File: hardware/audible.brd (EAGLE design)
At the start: 27.7 x 23.4 mm, 5 parts, among them J1 SQUALL_HEADER, J2 HIROSE-DF40C-10DP-0.4V, J3 HIROSE-DF40C-10DP-0.4V, J5 TC2030-JLINK-NL

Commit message: Almost completed schematic
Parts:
- added C1, C2, C3: 1uF, passives:0402_CAP
- added C4: 100n, passives:0402_CAP
- added C5: 1u, passives:0402_CAP
- added C6: 22uF, passives:0402_CAP
- added IC1: LTC1966CMS8, chips:MSOP8
- added R1, R4: 14k, passives:0402_RES
- added R2, R5: 1k, passives:0402_RES
- added R3: 47k, passives:0402_RES
- added R6: 20k, passives:0402_RES
- added R7, R8, R9: 10k, passives:0402_RES
- added U$2: ICS-40310, chips:LGA_CAV3
- added U$3: LD39015, chips:SOT-23-5
- added U1, U2: MAX417ESA+, chips:21-0041B_8
- moved U$1 7.26 mm to (13.8, 8.79)
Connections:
- new net MIC: C3.1, U$2.P$3
- new net MIC_AMP_1: R1.2, U1.1, U1.5
- new net MIC_AMP_2: C4.1, R4.1, U1.7
- new net N$1: C3.2, R3.2, U1.3
- new net N$10: C6.2, R6.2, R7.1, U2.5
- new net N$2: C4.2, IC1.2
- new net N$4: R1.1, R2.2, U1.2
- new net N$5: R4.2, R5.1, U1.6
- new net N$6: R8.1, U2.6
- new net RMS: C5.2, IC1.5, U2.3
- new net RMS_BUF: R6.1, U2.1, U2.2
- new net VREF: C1.1, IC1.3, R2.1, R3.1, R5.2, U$2.P$1, U$3.5
- net A7: now also R7.2, R9.1, U2.7
- net GND: now also C1.2, C2.2, C5.1, C6.1, IC1.1, IC1.4, IC1.6, R8.2, R9.2, U$2.P$2, U$3.2, U1.4, U2.4
- net P23: now also IC1.8
- net VCC: now also C2.1, IC1.7, U$3.1, U1.8, U2.8
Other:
- board text removed: "2016/03/12"
- board text removed: "Accel"
- board text removed: "BLEES"
- board text removed: "D"
- board text removed: "Ghena, Bertoldi, Jones, Pratt, Su"
- board text removed: "Light"
- board text removed: "Pressure"
- board text removed: "Temp Humid"

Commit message: better layout
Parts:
- added C7: 0.01uF, passives:0402_CAP
- added C8: 0.1uF, passives:0402_CAP
- moved IC1 31.1 mm to (19.7, 18.5)
- moved U$3 23.9 mm to (17.2, 8.71), turned to 90 degrees
- moved U1 20.0 mm to (23.8, 10.3), turned to 90 degrees
- moved U2 16.8 mm to (31.5, 16.6), turned to 90 degrees
- moved R4 10.8 mm to (27.8, 11.7)
- moved C3 10.1 mm to (26.7, 5.44), turned to 90 degrees
- moved R8 9.59 mm to (34.7, 14.4), turned to 270 degrees
- moved R3 9.49 mm to (19.1, 3.30), turned to 90 degrees
- moved R1 9.36 mm to (28.4, 5.44), turned to 90 degrees
- moved R6 9.34 mm to (27.4, 19.3)
- moved C5 8.18 mm to (20.5, 15.4), turned to 90 degrees
- moved C6 8.18 mm to (27.3, 15.6), turned to 90 degrees
- moved R9 7.97 mm to (34.7, 17.0), turned to 270 degrees
- moved R7 7.34 mm to (27.4, 17.5)
- moved C1 7.25 mm to (18.5, 5.69), turned to 90 degrees
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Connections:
- net GND: now also C7.1, C8.2
- net VCC: now also C7.2
- net VREF: now also C8.1

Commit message: better schematic
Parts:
- added Q1: FK3503010L, chips:SC85
- moved U$1 17.9 mm to (29.9, 3.66)
- moved R1 10.6 mm to (19.3, 10.9), turned to 180 degrees
- moved R2 5.87 mm to (19.3, 8.79), turned to 180 degrees
- moved C8 4.34 mm to (22.1, 2.44)
- moved R6 4.34 mm to (27.5, 14.9), turned to 90 degrees
- moved C7 3.79 mm to (24.3, 19.1)
- moved C1 3.69 mm to (15.1, 7.11)
- moved U$3 2.00 mm to (15.6, 9.91)
- moved C3 1.68 mm to (27.4, 3.91)
- moved C6 1.63 mm to (27.4, 17.2)
- moved R7 1.63 mm to (27.4, 19.1)
- moved C2 1.44 mm to (16.5, 7.09), turned to 270 degrees
- moved C5 1.37 mm to (21.8, 15.7)
- moved R4 0.98 mm to (27.3, 12.5), turned to 270 degrees
- moved C4 0.84 mm to (19.2, 15.2)
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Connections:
- net GND: now also Q1.2
- net N$10: now also Q1.3
- net P22: now also U$3.3
- net P24: now also Q1.1

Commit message: Updated sch and brd
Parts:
- added C10, C9: 0.1uF, passives:0402_CAP
- moved C2 7.61 mm to (20.0, 13.9), turned to 180 degrees
- moved R7 7.40 mm to (30.9, 12.6)
- moved C1 6.34 mm to (19.2, 2.34), turned to 270 degrees
- moved C4 5.26 mm to (15.5, 18.9)
- moved C6 4.26 mm to (25.8, 13.3), turned to 270 degrees
- moved R2 3.59 mm to (17.4, 5.71), turned to 0 degrees
- moved R1 3.46 mm to (19.5, 7.42), turned to 0 degrees
- moved U2 2.64 mm to (28.9, 17.0), turned to 0 degrees
- moved R6 2.61 mm to (28.7, 12.6), turned to 0 degrees
- moved Q1 2.51 mm to (22.8, 14.2)
- moved C5 2.42 mm to (24.1, 16.6)
- moved R8 2.33 mm to (33.4, 16.3), turned to 0 degrees
- moved R5 2.27 mm to (26.5, 8.13)
- moved U1 2.22 mm to (23.1, 8.23)
- moved R4 2.15 mm to (26.5, 10.5)
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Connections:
- net RMS renamed N$3
- net GND: now also C10.1, C9.1
- net MIC: now also U$2.P$1; no longer U$2.P$3
- net VCC: now also C10.2, C9.2
- net VREF: now also U$2.P$3; no longer U$2.P$1
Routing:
- net GND: track 4.95 -> 0.00 mm, vias 3 -> 0

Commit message: almost routed
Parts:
- moved C10 14.0 mm to (24.1, 18.4), turned to 90 degrees
- moved C9 10.9 mm to (21.0, 15.2), turned to 180 degrees
- moved C1 7.67 mm to (14.6, 8.43), turned to 180 degrees
- moved C4 7.22 mm to (22.3, 16.5), turned to 180 degrees
- moved Q1 6.81 mm to (29.2, 11.9), turned to 0 degrees
- moved R4 5.19 mm to (23.0, 14.3), turned to 0 degrees
- moved C6 3.78 mm to (29.3, 14.7)
- moved R5 3.73 mm to (26.5, 11.9)
- moved R6 3.68 mm to (31.9, 14.4)
- moved C3 3.56 mm to (24.0, 5.74), turned to 0 degrees
- moved C8 2.70 mm to (19.5, 2.67), turned to 0 degrees
- moved R3 2.69 mm to (22.0, 4.57), turned to 90 degrees
- moved R2 2.39 mm to (19.5, 4.50)
- moved U1 1.94 mm to (22.9, 10.2)
- moved C7 1.29 mm to (25.1, 19.7)
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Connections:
- net A5: no longer J3.9
- net A6: no longer J3.7
- net MISO: no longer J3.8
- net MOSI: no longer J3.6
- net P25: no longer J2.8
- net SCL: no longer J3.3
- net SCLK: no longer J3.10
- net SDA: no longer J3.1
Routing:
- net GND: track 0.00 -> 48.6 mm, vias 0 -> 7
- net VREF: track 0.00 -> 47.2 mm, vias 0 -> 2
- net VCC: track 0.00 -> 38.4 mm, vias 0 -> 4
- net A7: track 0.00 -> 18.3 mm, vias 0 -> 1
- net P24: track 0.00 -> 16.6 mm, vias 0 -> 3
- net SWDIO/!RESET: track 0.00 -> 13.5 mm, vias 0 -> 2
- net 5V: track 0.00 -> 13.5 mm, vias 0 -> 2
- net P23: track 0.00 -> 12.7 mm, vias 0 -> 3
- net P22: track 0.00 -> 10.4 mm, vias 0 -> 1
- net MIC_AMP_1: track 0.00 -> 9.03 mm
- net RMS_BUF: track 0.00 -> 8.09 mm
- net SWDCLK: track 0.00 -> 8.00 mm, vias 0 -> 1
- net N$10: track 0.00 -> 7.44 mm
- net N$4: track 0.00 -> 6.19 mm
- net N$5: track 0.00 -> 6.00 mm
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
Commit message: routed
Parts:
- moved C4 4.72 mm to (18.7, 13.5)
- moved U$3 2.76 mm to (17.3, 7.95)
- moved C2 2.46 mm to (19.8, 11.1)
- moved C9 2.14 mm to (21.5, 13.1)
- moved R5 1.41 mm to (26.1, 13.2), turned to 0 degrees
- moved Q1 1.24 mm to (28.1, 11.4)
- moved R4 1.18 mm to (23.3, 13.2)
- moved U1 1.16 mm to (23.5, 9.17)
- moved C3 0.99 mm to (24.6, 4.98)
- moved IC1 0.97 mm to (20.6, 17.5)
- moved C6 0.94 mm to (29.0, 13.8)
- moved R8 0.91 mm to (33.5, 16.7)
- moved R9 0.91 mm to (34.3, 17.9)
- moved U2 0.89 mm to (29.0, 17.3)
- moved C10 0.89 mm to (23.8, 17.5)
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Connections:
- removed net A5: J1.B9
- removed net A6: J1.B7
- removed net MISO: J1.B8
- removed net MOSI: J1.B6
- removed net P25: J1.A8
- removed net SCL: J1.B3
- removed net SCLK: J1.B10
- removed net SDA: J1.B1
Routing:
- net GND: track 48.6 -> 105.1 mm, vias 7 -> 12
- net VCC: track 38.4 -> 62.3 mm, vias 4 -> 3
- net MIC_AMP_2: track 4.03 -> 8.24 mm, vias 0 -> 2
- net P22: track 10.4 -> 14.3 mm
- net P23: track 12.7 -> 15.8 mm, vias 3 -> 1
- net 5V: track 13.5 -> 16.0 mm, vias 2 -> 1
- net N$5: track 6.00 -> 3.66 mm
- net N$2: track 4.34 -> 6.02 mm
- net VREF: track 47.2 -> 48.6 mm
- net N$3: track 5.06 -> 3.95 mm
- net P24: track 16.6 -> 17.7 mm, vias 3 -> 2
- net RMS_BUF: track 8.09 -> 8.89 mm
- net N$10: track 7.44 -> 6.81 mm

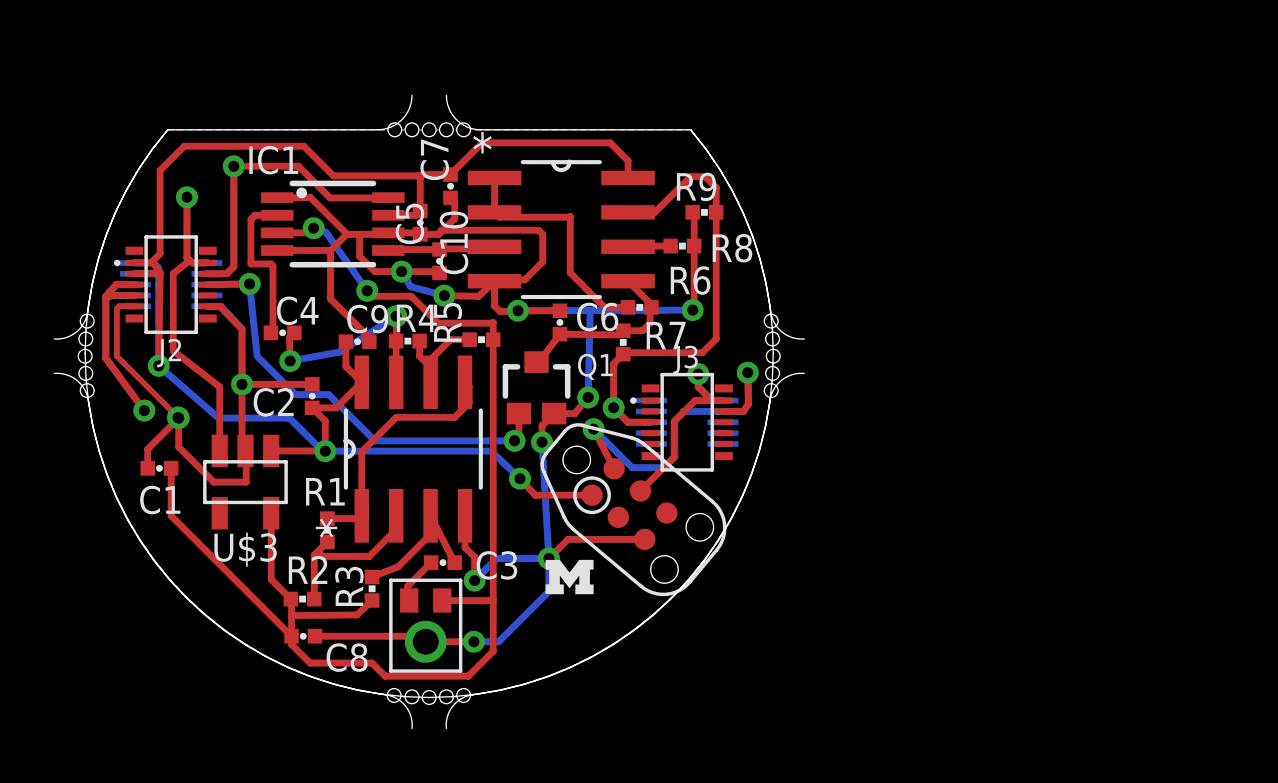
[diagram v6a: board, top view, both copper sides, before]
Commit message: fixed clearance issues from wrong wire width
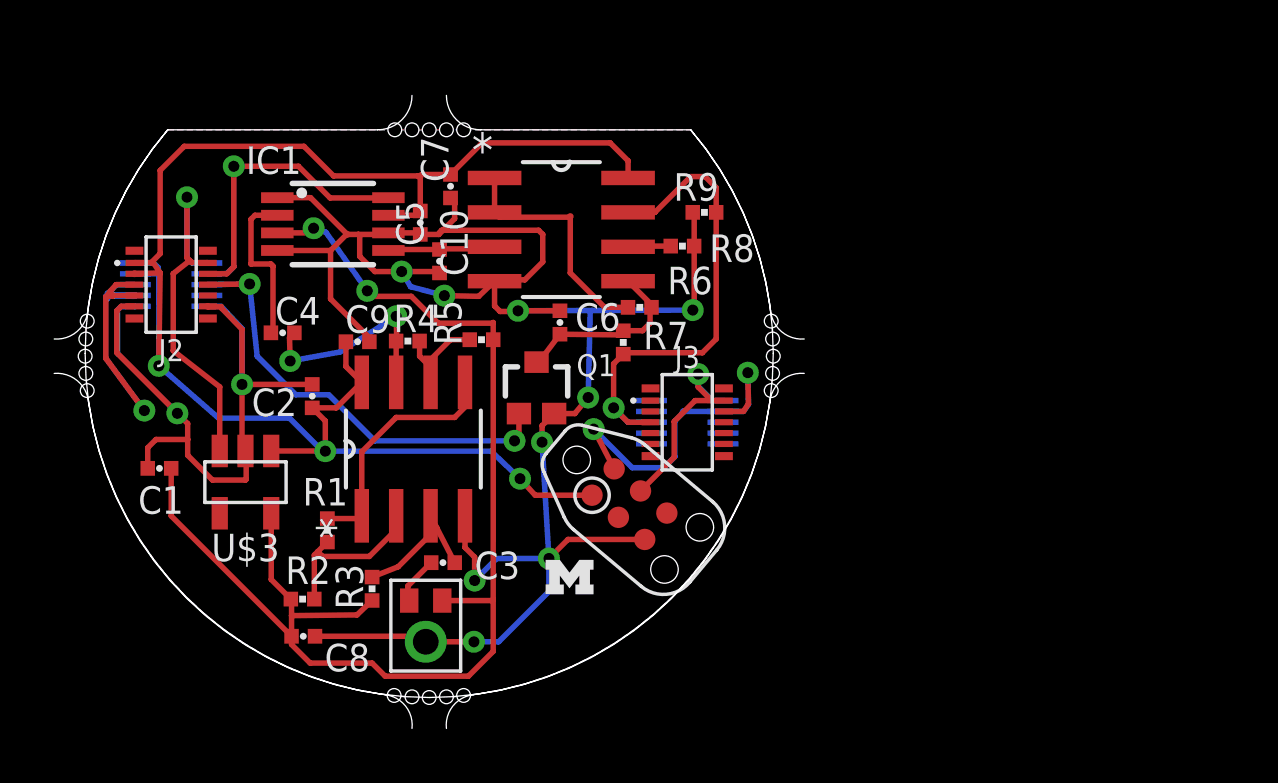
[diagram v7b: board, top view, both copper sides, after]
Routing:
- net GND: track 105.1 -> 104.7 mm, vias 12 -> 11

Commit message: Removed headers and fixed wire angles
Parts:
- removed J2, J3: HIROSE-DF40C-10DP-0.4V, headers:2X5/SMD/0.4MM
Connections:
- net 5V: no longer J2.5, J2.7
- net A7: no longer J3.5
- net GND: no longer J2.10, J2.9
- net P22: no longer J2.2
- net P23: no longer J2.4
- net P24: no longer J2.6
- net SWDCLK: no longer J3.2
- net SWDIO/!RESET: no longer J3.4
- net VCC: no longer J2.1, J2.3
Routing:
- net 5V: track 16.0 -> 0.40 mm, vias 1 -> 0
- net GND: track 104.7 -> 89.4 mm
- net P22: track 14.3 -> 8.35 mm
- net VCC: track 62.3 -> 56.8 mm, vias 3 -> 4
- net P23: track 15.8 -> 11.0 mm
- net SWDIO/!RESET: track 13.1 -> 8.53 mm, vias 2 -> 1
- net A7: track 18.7 -> 17.1 mm
- net SWDCLK: track 8.00 -> 6.66 mm
- net P24: track 17.7 -> 16.3 mm
- net RMS_BUF: track 8.89 -> 8.26 mm
